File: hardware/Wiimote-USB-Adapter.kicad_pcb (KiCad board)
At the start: 2 copper layers, 45 x 35 mm, 20 parts, among them J101 LED_Left, J102 LED_Right, SW101 SYNC, U101 J27H002, U102 LM1117-3.3

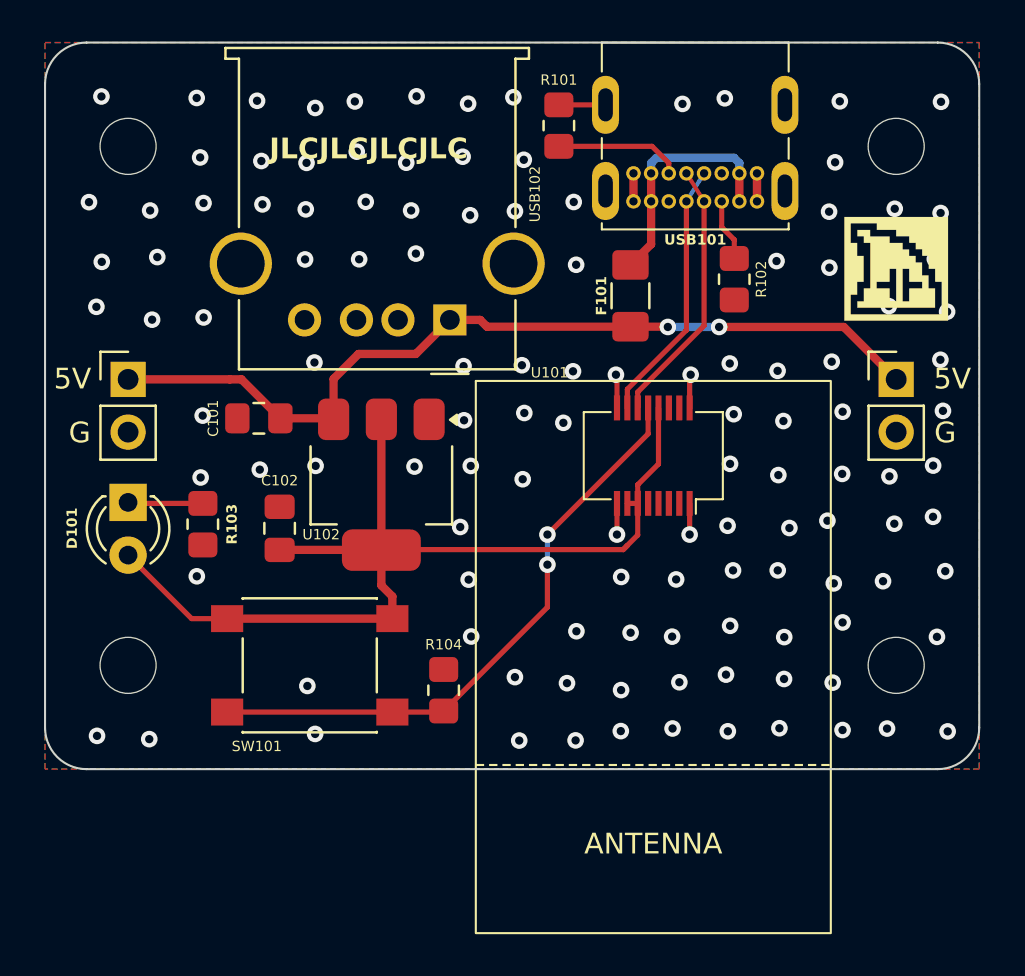
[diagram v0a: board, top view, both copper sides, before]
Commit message: Clean up silkscreen and vias
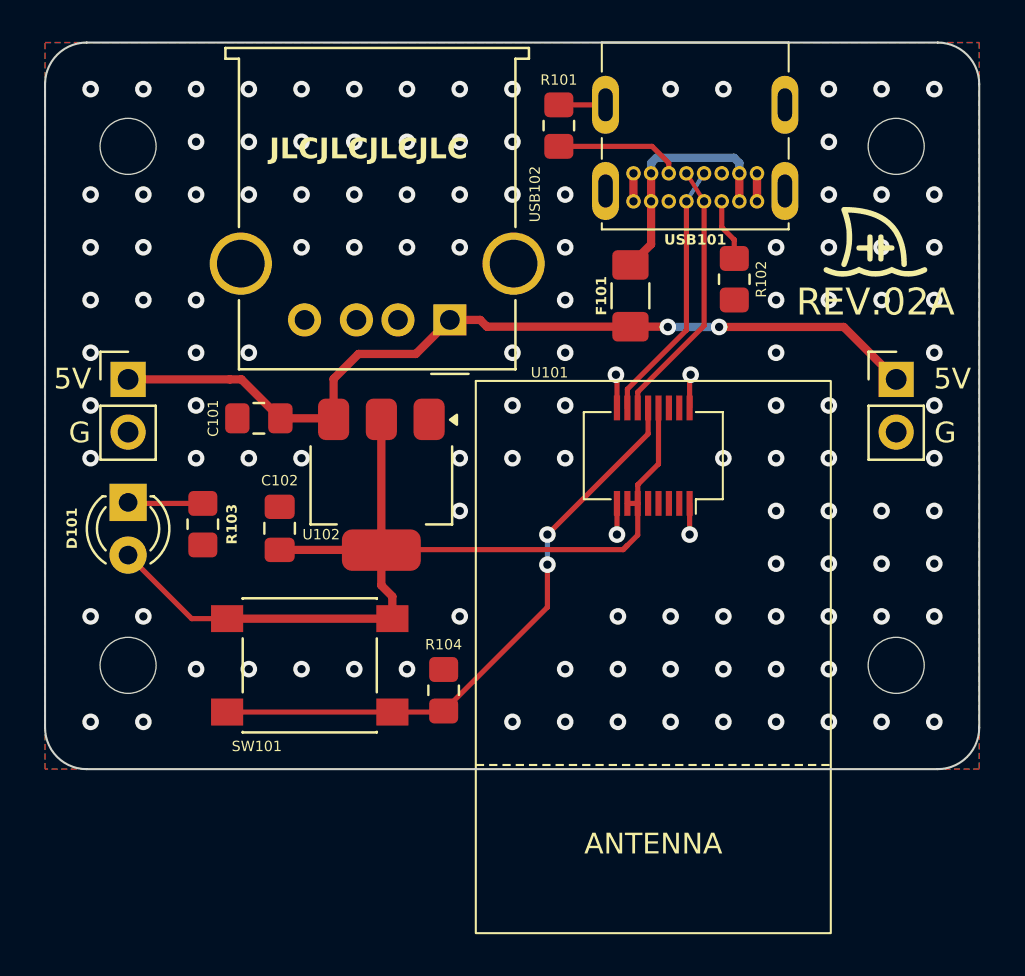
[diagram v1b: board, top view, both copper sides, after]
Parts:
- removed the G*** at (157.5, 86.9)
- added G***: LOGO, Logos:Embedded-Shark-Logo-Inverted-5mm, F.Cu at (156.5, 85.5)
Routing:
- net GND: vias 122 -> 124
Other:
- board text added: "REV.${REVISION}"
- board text removed: "${PROJECTNAME} REV.${REVISION} ${COMPANY} ${ISSUE_DATE}"

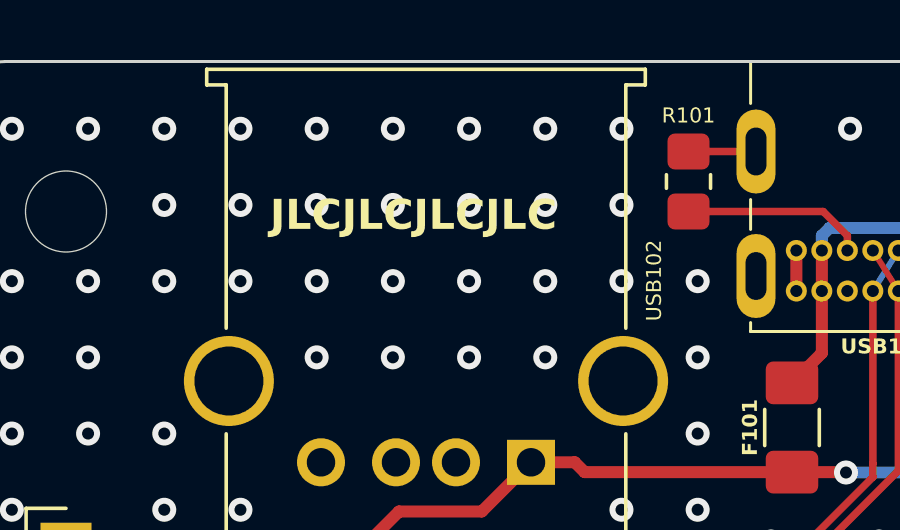
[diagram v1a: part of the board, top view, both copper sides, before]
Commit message: Remove PCB markings
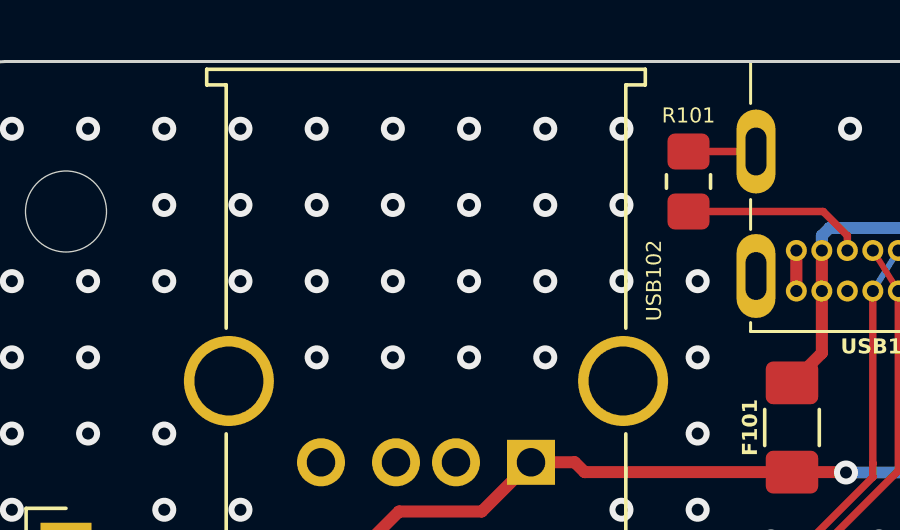
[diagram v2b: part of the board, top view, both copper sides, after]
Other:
- board text removed: "JLCJLCJLCJLC"
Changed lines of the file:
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@@
 	(title_block
 		(title "Wiimote-USB-Adapter")
-		(date "2024-09-14")
+		(date "2024-11-23")
 		(rev "02A")
 		(company "Embedded Shark, LLC")
@@
 		)
 	)
-	(gr_text "JLCJLCJLCJLC"
-		(at 127.3 81.7 0)
-		(layer "F.SilkS")
-		(effects
-			(font
-				(size 1 1)
-				(thickness 0.1)
-				(bold yes)
-			)
-			(justify left bottom)
-		)
-	)
